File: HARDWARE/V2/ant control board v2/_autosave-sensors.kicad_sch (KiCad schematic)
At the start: 11 parts, among them J1 SWITCH, J2 2s Battery, J3 USB-C_304A-ACP16X, U1 GM7333

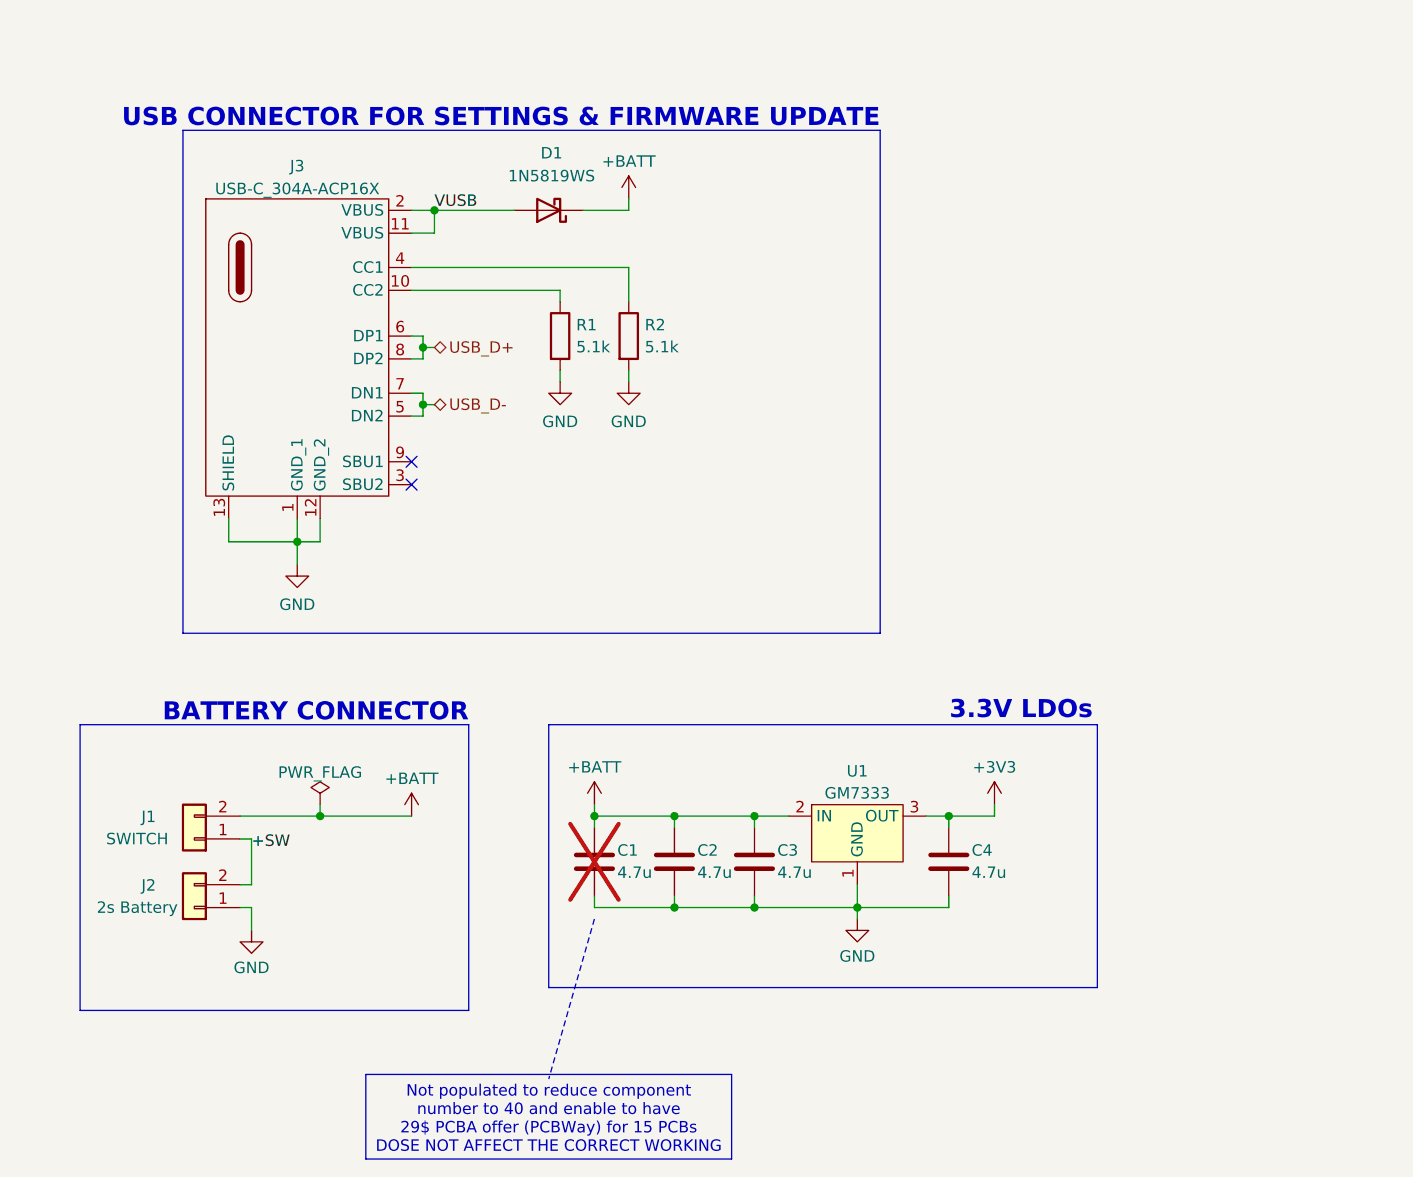
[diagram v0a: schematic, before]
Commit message: Adjusted some pcb things and re generated Prouction files
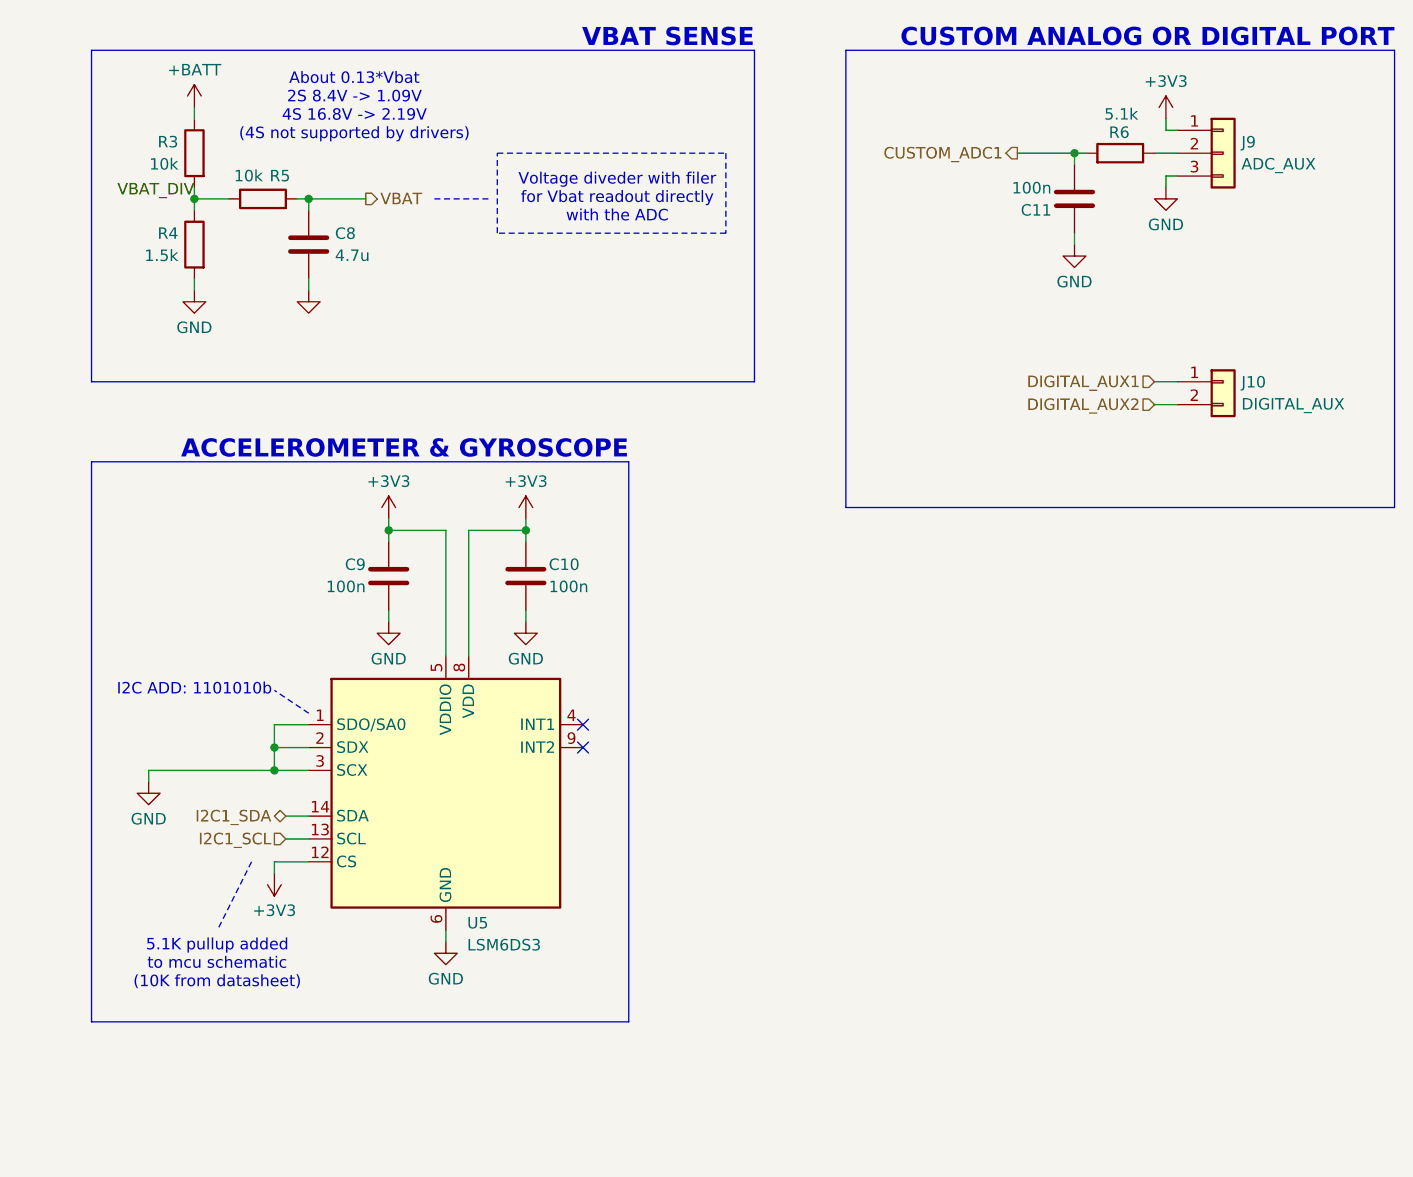
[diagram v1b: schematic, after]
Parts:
- removed C1, C2, C3, C4: 4.7u, Capacitor_SMD:C_0402_1005Metric, symbol Device:C
- removed D1: 1N5819WS, Diode_SMD:D_SOD-323, symbol Device:D_Schottky
- removed J1: SWITCH, _MY_connectors:01x02_TH_pad_renforced, symbol Connector_Generic:Conn_01x02
- removed J2: 2s Battery, _MY_connectors:01x02_TH_pad_renforced, symbol Connector_Generic:Conn_01x02
- removed J3: USB-C_304A-ACP16X, _MIA footprint:USB_C_304A-ACP16X, symbol _MIA:USB-C_304A-ACP16X
- removed R1, R2: 5.1k, Resistor_SMD:R_0402_1005Metric, symbol Device:R
- removed U1: GM7333, Package_TO_SOT_SMD:SOT-89-3, symbol _My_power_management_IC:GM7333
- added C10, C11, C9: 100n, Capacitor_SMD:C_0402_1005Metric, symbol Device:C
- added C8: 4.7u, Capacitor_SMD:C_0402_1005Metric, symbol Device:C
- added J10: DIGITAL_AUX, _MY_connectors:01x02_TH_pad_renforced_small, symbol Connector_Generic:Conn_01x02
- added J9: ADC_AUX, _MY_connectors:01x03_TH_pad_renforced_small, symbol Connector_Generic:Conn_01x03
- added R3, R5: 10k, Resistor_SMD:R_0402_1005Metric, symbol Device:R
- added R4: 1.5k, Resistor_SMD:R_0402_1005Metric, symbol Device:R
- added R6: 5.1k, Resistor_SMD:R_0402_1005Metric, symbol Device:R
- added U5: LSM6DS3, Package_LGA:LGA-14_3x2.5mm_P0.5mm_LayoutBorder3x4y, symbol Sensor_Motion:LSM6DS3
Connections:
- net +3V3: now also C10.1, C9.1, J9.1 (Pin_1), U5.12 (CS), U5.5 (VDDIO), U5.8 (VDD)
- net +BATT: now also R3.1
- net GND: now also C10.2, C11.1, C8.1, C9.2, J9.3 (Pin_3), R4.2, U5.1 (SDO/SA0), U5.2 (SDX), U5.3 (SCX), U5.6 (GND), U5.7 (GND)
- new net: J9.2 (Pin_2), R6.1
- new net CUSTOM_ADC1: C11.2, R6.2
- new net DIGITAL_AUX1: J10.1 (Pin_1)
- new net DIGITAL_AUX2: J10.2 (Pin_2)
- new net I2C1_SCL: U5.13 (SCL)
- new net I2C1_SDA: U5.14 (SDA)
- new net VBAT: C8.2, R5.2
- new net VBAT_DIV: R3.2, R4.1, R5.1
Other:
- note added: "5.1K pullup added to mcu schematic (10K from datasheet)"
- note added: "ACCELEROMETER & GYROSCOPE"
- note added: "About 0.13*Vbat 2S 8.4V -> 1.09V 4S 16.8V -> 2.19V (4S not supported by drivers)"
- note added: "CUSTOM ANALOG OR DIGITAL PORT"
- note added: "I2C ADD: 1101010b"
- note added: "VBAT SENSE"
- note added: "Voltage diveder with filer for Vbat readout directly with the ADC"
- note removed: "3.3V LDOs"
- note removed: "BATTERY CONNECTOR"
- note removed: "Not populated to reduce component number to 40 and enable to have 29$ PCBA offer (PCBWay) for 15 PCBs DOSE NOT AFFECT THE CORRECT WORKING"
- note removed: "USB CONNECTOR FOR SETTINGS & FIRMWARE UPDATE"
